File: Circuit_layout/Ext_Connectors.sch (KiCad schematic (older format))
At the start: 12 parts, among them CON1 AVR-JTAG-10, J1 Spare_Conns, J4 Motor_Ctrl, J5 RJ12, P1 TSV, P2 CONN_02X10, P3 CONN_02X07, U14 Mounting_hole, U15 Mounting_hole, U25 Mounting_hole, U26 Mounting_hole

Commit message: Generated gerber and drill files for board ordering
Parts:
- removed P2: CONN_02X10, Connect:IDC_Header_Straight_20pins, symbol CONN_02X10
- removed P3: CONN_02X07, Connect:IDC_Header_Straight_14pins, symbol CONN_02X07
- added J1: Pedal_Cluster, Connectors_Molex:Molex_MiniFit-JR-5556-12A_2x06x4.20mm_Straight, symbol Conn_01x12
- added J10: Can_Iso, Connectors_Molex:Molex_MiniFit-JR-5556-04A_2x02x4.20mm_Straight, symbol Conn_01x04
- added J11: AIRs, Connectors_Molex:Molex_MiniFit-JR-5556-02A_2x01x4.20mm_Straight, symbol Conn_01x02
- added J12: IMD_Relay, Connectors_Molex:Molex_MiniFit-JR-5556-02A_2x01x4.20mm_Straight, symbol Conn_01x02
- added J2: Lights, Connectors_Molex:Molex_MiniFit-JR-5556-10A_2x05x4.20mm_Straight, symbol Conn_01x10
- added J3: Cockpit, Connectors_Molex:Molex_MiniFit-JR-5556-08A_2x04x4.20mm_Straight, symbol Conn_01x08
- added J7: GLV_In, Connectors_Molex:Molex_MiniFit-JR-5556-06A_2x03x4.20mm_Straight, symbol Conn_01x06
- added J8: GLV_Out, Connectors_Molex:Molex_MiniFit-JR-5556-06A_2x03x4.20mm_Straight, symbol Conn_01x06
- added J9: IMD, custom_footprints:IMD_Header, symbol Conn_01x08
- renumbered P1 to J13, J1 to J6
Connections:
- net +24V: now also J7.5 (Pin_5), J8.5 (Pin_5), J9.2 (Pin_2)
- net +24V_RTN: now also J7.6 (Pin_6), J8.6 (Pin_6)
- net +5V: now also J3.3 (Pin_3)
- net AIRs+: now also J11.1 (Pin_1)
- net AIRs-: now also J11.2 (Pin_2)
- net APPS1: now also J1.6 (Pin_6)
- net APPS1_10: now also J1.5 (Pin_5)
- net APPS1_RTN: now also J1.7 (Pin_7)
- net APPS2: now also J1.9 (Pin_9)
- net APPS2_5: now also J1.8 (Pin_8)
- net BP: now also J1.3 (Pin_3), J2.1 (Pin_1)
- net Brake_24: now also J1.1 (Pin_1), J1.2 (Pin_2)
- net CANH: now also J10.1 (Pin_1), J7.1 (Pin_1), J8.1 (Pin_1)
- net CANL: now also J10.2 (Pin_2), J7.2 (Pin_2), J8.2 (Pin_2)
- net Drive_BTN: now also J3.4 (Pin_4)
- net Drive_LED: now also J3.5 (Pin_5)
- net GND: now also J10.3 (Pin_3), J12.2 (Pin_2), J2.2 (Pin_2), J2.4 (Pin_4), J2.6 (Pin_6), J2.8 (Pin_8), J3.1 (Pin_1), J3.8 (Pin_8), J7.3 (Pin_3), J7.4 (Pin_4), J8.3 (Pin_3), J8.4 (Pin_4), J9.1 (Pin_1), J9.3 (Pin_3), J9.4 (Pin_4)
- net HVPL: now also J2.3 (Pin_3), J2.5 (Pin_5), J3.6 (Pin_6)
- net IMD_Fault_LED: now also J3.2 (Pin_2)
- net IMD_PWM: now also J9.5 (Pin_5)
- net IMD_Status: now also J12.1 (Pin_1), J9.8 (Pin_8)
- net RTDS: now also J2.7 (Pin_7)
- net RTN_GLV: now also J1.10 (Pin_10)
- new net SPARE_LED: J3.7 (Pin_7)
- no-connect marks 9 -> 14
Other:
- note removed: "AIRs"
- note removed: "CAN Bus"
- note removed: "GLV"
- note removed: "HVPL"
- note removed: "IMD"
- note removed: "On current board PIN19 is tied to PIN20 of P2. \nThis due to BOT and BP needing +24V."
- note removed: "PIN1 and PIN3 tied, due to voltage regulator used (LM7810).\nSee note on Throttle Plausibiliy sheet."
- note removed: "Pedals"
- moved on the sheet: +24V1, CON1, J5, J6

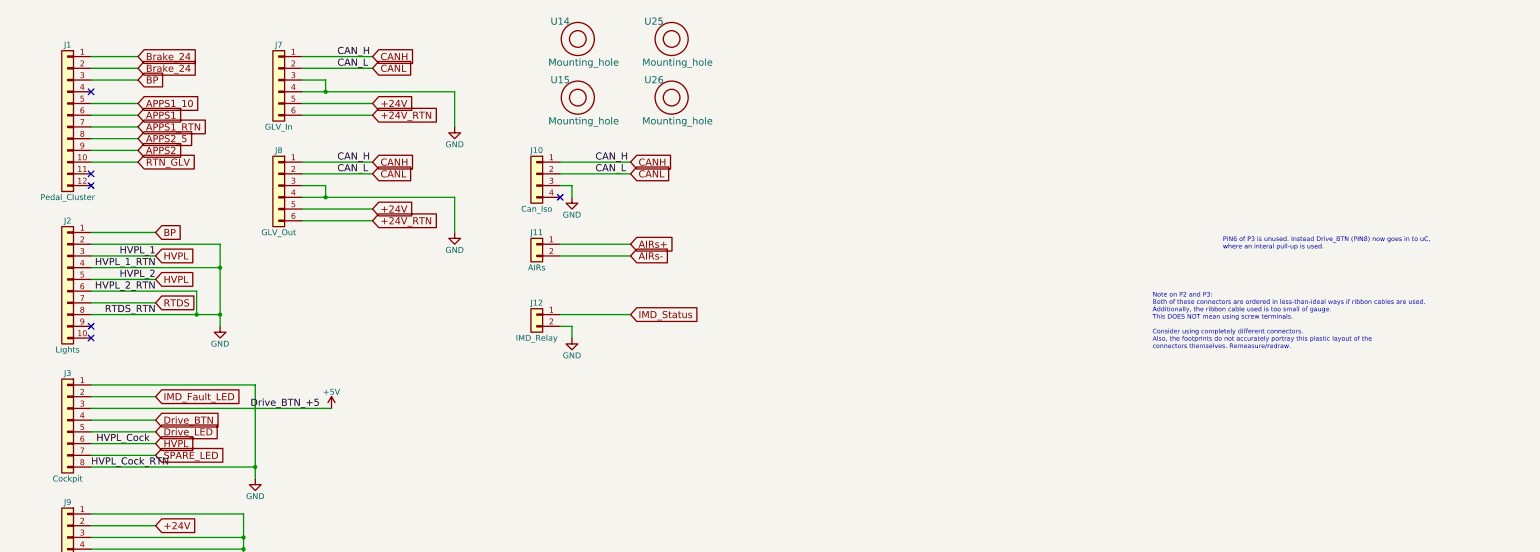
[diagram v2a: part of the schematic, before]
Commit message: Schematic update
Changed schematic to reflect board as assembeled
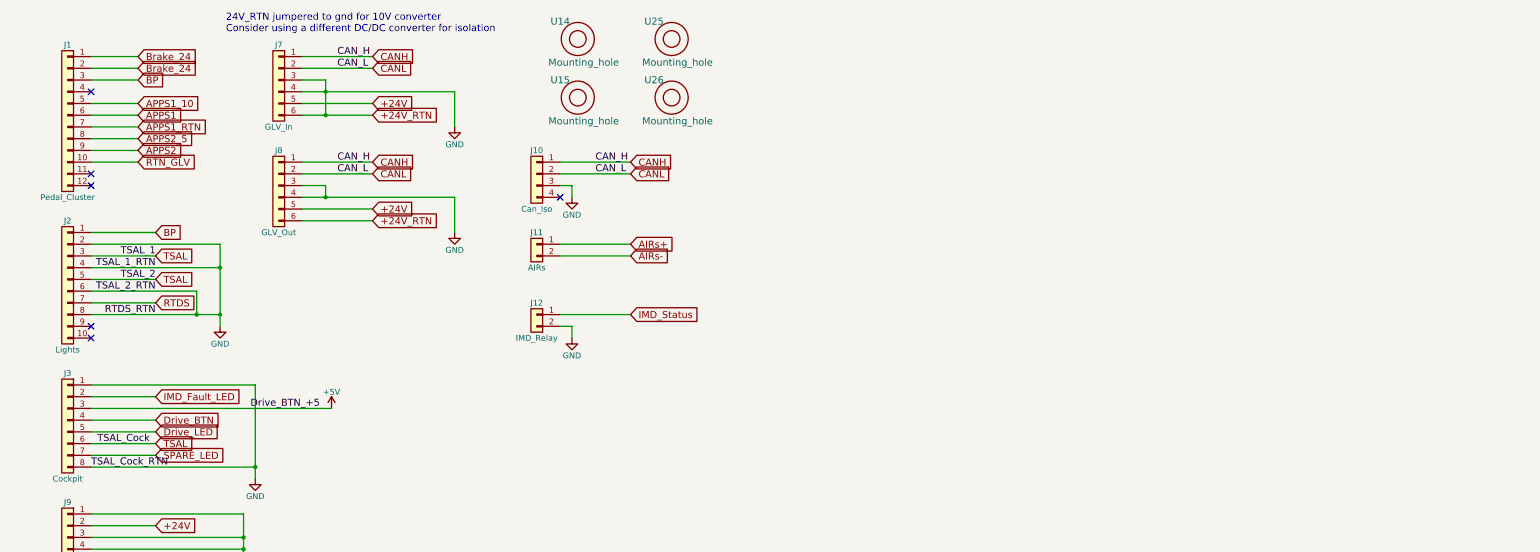
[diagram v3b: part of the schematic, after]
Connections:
- net +24V_RTN is gone; now on net GND: J7.6 (Pin_6), J8.6 (Pin_6)
- net HVPL renamed TSAL
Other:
- note added: "24V_RTN jumpered to gnd for 10V converter\nConsider using a different DC/DC converter for isolation"
- note removed: "Note on P2 and P3:\nBoth of these connectors are ordered in less-than-ideal ways if ribbon cables are used.\nAdditionally, the ribbon cable used is too small of gauge.\nThis DOES NOT mean using screw terminals.\n\nConsider using completely different connectors.\nAlso, the footprints do not accurately portray this plastic layout of the\nconnectors themselves. Remeasure/redraw."
- note removed: "PIN6 of P3 is unused. Instead Drive_BTN (PIN8) now goes in to uC,\nwhere an interal pull-up is used."
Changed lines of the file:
@@
 LIBS:ftdi
 LIBS:gennum
-LIBS:graphic
 LIBS:hc11
 LIBS:intel
@@
 LIBS:Lattice
 LIBS:linear
-LIBS:logo
 LIBS:maxim
 LIBS:memory
@@
 $EndDescr
 Text Label 5650 2600 2    60   ~ 0
-HVPL_1
+TSAL_1
 Text Label 5650 2700 2    60   ~ 0
-HVPL_1_RTN
+TSAL_1_RTN
 Text Label 5650 2800 2    60   ~ 0
-HVPL_2
+TSAL_2
 Text Label 5650 2900 2    60   ~ 0
-HVPL_2_RTN
+TSAL_2_RTN
 $Comp
 L CONN_01X04 J4
@@
 IMD_PWM
 Text GLabel 5650 2600 2    60   Input ~ 0
-HVPL
+TSAL
 Text GLabel 5650 2800 2    60   Input ~ 0
-HVPL
+TSAL
 Text GLabel 3200 2000 3    60   Input ~ 0
 A2_LV
@@
 $EndComp
 Text GLabel 5650 4200 2    60   Input ~ 0
-HVPL
+TSAL
 Text GLabel 7500 900  2    60   Input ~ 0
 CANH
@@
 $EndComp
 Text Label 5600 4200 2    60   ~ 0
-HVPL_Cock
+TSAL_Cock
 Text Label 5100 4400 0    60   ~ 0
-HVPL_Cock_RTN
+TSAL_Cock_RTN
 $Comp
 L Mounting_hole U14
@@
 	1    0    0    -1
 $EndComp
-Text Notes 14750 2550 0    39   ~ 0
-PIN6 of P3 is unused. Instead Drive_BTN (PIN8) now goes in to uC,\nwhere an interal pull-up is used.
-Text Notes 14150 3400 0    39   ~ 0
-Note on P2 and P3:\nBoth of these connectors are ordered in less-than-ideal ways if ribbon cables are used.\nAdditionally, the ribbon cable used is too small of gauge.\nThis DOES NOT mean using screw terminals.\n\nConsider using completely different connectors.\nAlso, the footprints do not accurately portray this plastic layout of the\nconnectors themselves. Remeasure/redraw.
 $Comp
 L Conn_01x12 J1
@@
 	6900 1100 7100 1100
 Wire Wire Line
-	7100 1100 7100 1200
+	7100 1100 7100 1400
 Connection ~ 7100 1200
 Wire Wire Line
@@
 	5100 4300 5650 4300
 NoConn ~ 5100 1200
+Connection ~ 7100 1400
+Text Notes 6250 700  0    60   ~ 0
+24V_RTN jumpered to gnd for 10V converter\nConsider using a different DC/DC converter for isolation
 $EndSCHEMATC
